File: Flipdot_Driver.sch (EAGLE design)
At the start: 27 parts

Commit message: Finished driver board design
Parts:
- added U$6: 3_PIN, Flipdot:3_PIN
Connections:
- net A: now also U$6.1
- net B: now also U$6.2
- net C: now also U$6.3
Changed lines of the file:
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@@
 <part name="U$11" library="Flipdot" deviceset="4_PIN" device=""/>
 <part name="U$5" library="Flipdot" deviceset="3_PIN" device=""/>
+<part name="U$6" library="Flipdot" deviceset="3_PIN" device=""/>
 </parts>
 <sheets>
@@
 <instance part="U$11" gate="G$1" x="-114.3" y="-144.78" rot="MR0"/>
 <instance part="U$5" gate="G$1" x="-22.86" y="-40.64" rot="MR0"/>
+<instance part="U$6" gate="G$1" x="-78.74" y="-2.54" rot="R180"/>
 </instances>
 <busses>
@@
 <label x="-40.64" y="7.62" size="1.778" layer="95"/>
 </segment>
+<segment>
+<pinref part="U$6" gate="G$1" pin="1"/>
+<wire x1="-60.96" y1="-7.62" x2="-73.66" y2="-7.62" width="0.1524" layer="91"/>
+<label x="-73.66" y="-7.62" size="1.778" layer="95"/>
+</segment>
 </net>
 <net name="B" class="0">
@@
 <wire x1="-38.1" y1="2.54" x2="-40.64" y2="2.54" width="0.1524" layer="91"/>
 <label x="-40.64" y="2.54" size="1.778" layer="95"/>
+</segment>
+<segment>
+<pinref part="U$6" gate="G$1" pin="2"/>
+<wire x1="-60.96" y1="-2.54" x2="-73.66" y2="-2.54" width="0.1524" layer="91"/>
+<label x="-73.66" y="-2.54" size="1.778" layer="95"/>
 </segment>
 </net>
@@
 <label x="-40.64" y="-2.54" size="1.778" layer="95"/>
 </segment>
-</net>
+<segment>
+<pinref part="U$6" gate="G$1" pin="3"/>
+<wire x1="-60.96" y1="2.54" x2="-73.66" y2="2.54" width="0.1524" layer="91"/>
+<label x="-73.66" y="2.54" size="1.778" layer="95"/>
+</segment>
+</net>

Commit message: Finished, sent for production review
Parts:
- removed U$6: 3_PIN, Flipdot:3_PIN
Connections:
- net A: no longer U$6.1
- net B: no longer U$6.2
- net C: no longer U$6.3
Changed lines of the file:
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@@
 <?xml version="1.0" encoding="utf-8"?>
 <!DOCTYPE eagle SYSTEM "eagle.dtd">
-<eagle version="9.1.3">
+<eagle version="9.2.2">
 <drawing>
 <settings>
@@
 <part name="U$11" library="Flipdot" deviceset="4_PIN" device=""/>
 <part name="U$5" library="Flipdot" deviceset="3_PIN" device=""/>
-<part name="U$6" library="Flipdot" deviceset="3_PIN" device=""/>
 </parts>
 <sheets>
@@
 </plain>
 <instances>
-<instance part="SUBSEG" gate="G$1" x="-15.24" y="-137.16" rot="R270"/>
-<instance part="COL_A_H" gate="G$1" x="66.04" y="-137.16" rot="R270"/>
-<instance part="COL_A_L" gate="G$1" x="66.04" y="-187.96" rot="R270"/>
-<instance part="COL_B_H" gate="G$1" x="66.04" y="-243.84" rot="R270"/>
-<instance part="COL_B_L" gate="G$1" x="66.04" y="-294.64" rot="R270"/>
-<instance part="COL_C_H" gate="G$1" x="66.04" y="-350.52" rot="R270"/>
-<instance part="COL_C_L" gate="G$1" x="66.04" y="-401.32" rot="R270"/>
-<instance part="COL_D_HL" gate="G$1" x="66.04" y="-457.2" rot="R270"/>
-<instance part="SOURCE_A" gate="G$1" x="124.46" y="-142.24" rot="R270"/>
-<instance part="SOURCE_B" gate="G$1" x="124.46" y="-248.92" rot="R270"/>
-<instance part="SOURCE_C" gate="G$1" x="124.46" y="-355.6" rot="R270"/>
-<instance part="SOURCE_D" gate="G$1" x="124.46" y="-462.28" rot="R270"/>
-<instance part="SINK_B" gate="G$1" x="124.46" y="-299.72" rot="R270"/>
-<instance part="SINK_C" gate="G$1" x="124.46" y="-406.4" rot="R270"/>
-<instance part="SINK_D" gate="G$1" x="124.46" y="-523.24" rot="R270"/>
-<instance part="SINK_A" gate="G$1" x="124.46" y="-193.04" rot="R270"/>
-<instance part="U$1" gate="G$1" x="302.26" y="-231.14" rot="R90"/>
-<instance part="ROW_L" gate="G$1" x="119.38" y="20.32" rot="R270"/>
-<instance part="ROW_H" gate="G$1" x="119.38" y="-33.02" rot="R270"/>
-<instance part="SINK_R" gate="G$1" x="172.72" y="10.16" rot="R270"/>
-<instance part="SOURCE_R" gate="G$1" x="172.72" y="-43.18" rot="R270"/>
-<instance part="U$2" gate="G$1" x="-33.02" y="2.54"/>
-<instance part="U$3" gate="G$1" x="-43.18" y="-124.46" rot="MR0"/>
-<instance part="U$4" gate="G$1" x="68.58" y="33.02" rot="R180"/>
-<instance part="U$10" gate="G$1" x="-81.28" y="-144.78"/>
-<instance part="U$11" gate="G$1" x="-114.3" y="-144.78" rot="MR0"/>
-<instance part="U$5" gate="G$1" x="-22.86" y="-40.64" rot="MR0"/>
-<instance part="U$6" gate="G$1" x="-78.74" y="-2.54" rot="R180"/>
+<instance part="SUBSEG" gate="G$1" x="-15.24" y="-137.16" smashed="yes" rot="R270">
+<attribute name="NAME" x="-20.32" y="-160.02" size="1.778" layer="94"/>
+</instance>
+<instance part="COL_A_H" gate="G$1" x="66.04" y="-137.16" smashed="yes" rot="R270">
+<attribute name="NAME" x="60.96" y="-160.02" size="1.778" layer="94"/>
+</instance>
+<instance part="COL_A_L" gate="G$1" x="66.04" y="-187.96" smashed="yes" rot="R270">
+<attribute name="NAME" x="60.96" y="-210.82" size="1.778" layer="94"/>
+</instance>
+<instance part="COL_B_H" gate="G$1" x="66.04" y="-243.84" smashed="yes" rot="R270">
+<attribute name="NAME" x="60.96" y="-266.7" size="1.778" layer="94"/>
+</instance>
+<instance part="COL_B_L" gate="G$1" x="66.04" y="-294.64" smashed="yes" rot="R270">
+<attribute name="NAME" x="60.96" y="-317.5" size="1.778" layer="94"/>
+</instance>
+<instance part="COL_C_H" gate="G$1" x="66.04" y="-350.52" smashed="yes" rot="R270">
+<attribute name="NAME" x="60.96" y="-373.38" size="1.778" layer="94"/>
+</instance>
+<instance part="COL_C_L" gate="G$1" x="66.04" y="-401.32" smashed="yes" rot="R270">
+<attribute name="NAME" x="60.96" y="-424.18" size="1.778" layer="94"/>
+</instance>
+<instance part="COL_D_HL" gate="G$1" x="66.04" y="-457.2" smashed="yes" rot="R270">
+<attribute name="NAME" x="60.96" y="-480.06" size="1.778" layer="94"/>
+</instance>
+<instance part="SOURCE_A" gate="G$1" x="124.46" y="-142.24" smashed="yes" rot="R270">
+<attribute name="NAME" x="119.38" y="-170.18" size="1.778" layer="94"/>
+</instance>
+<instance part="SOURCE_B" gate="G$1" x="124.46" y="-248.92" smashed="yes" rot="R270">
+<attribute name="NAME" x="119.38" y="-276.86" size="1.778" layer="94"/>
+</instance>
+<instance part="SOURCE_C" gate="G$1" x="124.46" y="-355.6" smashed="yes" rot="R270">
+<attribute name="NAME" x="119.38" y="-383.54" size="1.778" layer="94"/>
+</instance>
+<instance part="SOURCE_D" gate="G$1" x="124.46" y="-462.28" smashed="yes" rot="R270">
+<attribute name="NAME" x="119.38" y="-490.22" size="1.778" layer="94"/>
+</instance>
+<instance part="SINK_B" gate="G$1" x="124.46" y="-299.72" smashed="yes" rot="R270">
+<attribute name="NAME" x="119.38" y="-322.58" size="1.778" layer="94"/>
+</instance>
+<instance part="SINK_C" gate="G$1" x="124.46" y="-406.4" smashed="yes" rot="R270">
+<attribute name="NAME" x="119.38" y="-429.26" size="1.778" layer="94"/>
+</instance>
+<instance part="SINK_D" gate="G$1" x="124.46" y="-523.24" smashed="yes" rot="R270">
+<attribute name="NAME" x="119.38" y="-546.1" size="1.778" layer="94"/>
+</instance>
+<instance part="SINK_A" gate="G$1" x="124.46" y="-193.04" smashed="yes" rot="R270">
+<attribute name="NAME" x="119.38" y="-215.9" size="1.778" layer="94"/>
+</instance>
+<instance part="U$1" gate="G$1" x="302.26" y="-231.14" smashed="yes" rot="R90"/>
+<instance part="ROW_L" gate="G$1" x="119.38" y="20.32" smashed="yes" rot="R270">
+<attribute name="NAME" x="114.3" y="-2.54" size="1.778" layer="94"/>
+</instance>
+<instance part="ROW_H" gate="G$1" x="119.38" y="-33.02" smashed="yes" rot="R270">
+<attribute name="NAME" x="114.3" y="-55.88" size="1.778" layer="94"/>
+</instance>
+<instance part="SINK_R" gate="G$1" x="172.72" y="10.16" smashed="yes" rot="R270">
+<attribute name="NAME" x="167.64" y="-12.7" size="1.778" layer="94"/>
+</instance>
+<instance part="SOURCE_R" gate="G$1" x="172.72" y="-43.18" smashed="yes" rot="R270">
+<attribute name="NAME" x="167.64" y="-71.12" size="1.778" layer="94"/>
+</instance>
+<instance part="U$2" gate="G$1" x="-33.02" y="2.54" smashed="yes"/>
+<instance part="U$3" gate="G$1" x="-43.18" y="-124.46" smashed="yes" rot="MR0"/>
+<instance part="U$4" gate="G$1" x="68.58" y="33.02" smashed="yes" rot="R180"/>
+<instance part="U$10" gate="G$1" x="-81.28" y="-144.78" smashed="yes"/>
+<instance part="U$11" gate="G$1" x="-114.3" y="-144.78" smashed="yes" rot="MR0"/>
+<instance part="U$5" gate="G$1" x="-22.86" y="-40.64" smashed="yes" rot="MR0"/>
 </instances>
 <busses>
@@
 <label x="-40.64" y="7.62" size="1.778" layer="95"/>
 </segment>
-<segment>
-<pinref part="U$6" gate="G$1" pin="1"/>
-<wire x1="-60.96" y1="-7.62" x2="-73.66" y2="-7.62" width="0.1524" layer="91"/>
-<label x="-73.66" y="-7.62" size="1.778" layer="95"/>
-</segment>
 </net>
 <net name="B" class="0">
@@
 <wire x1="-38.1" y1="2.54" x2="-40.64" y2="2.54" width="0.1524" layer="91"/>
 <label x="-40.64" y="2.54" size="1.778" layer="95"/>
-</segment>
-<segment>
-<pinref part="U$6" gate="G$1" pin="2"/>
-<wire x1="-60.96" y1="-2.54" x2="-73.66" y2="-2.54" width="0.1524" layer="91"/>
-<label x="-73.66" y="-2.54" size="1.778" layer="95"/>
 </segment>
 </net>
@@
 <label x="-40.64" y="-2.54" size="1.778" layer="95"/>
 </segment>
-<segment>
-<pinref part="U$6" gate="G$1" pin="3"/>
-<wire x1="-60.96" y1="2.54" x2="-73.66" y2="2.54" width="0.1524" layer="91"/>
-<label x="-73.66" y="2.54" size="1.778" layer="95"/>
-</segment>
-</net>
+</net>

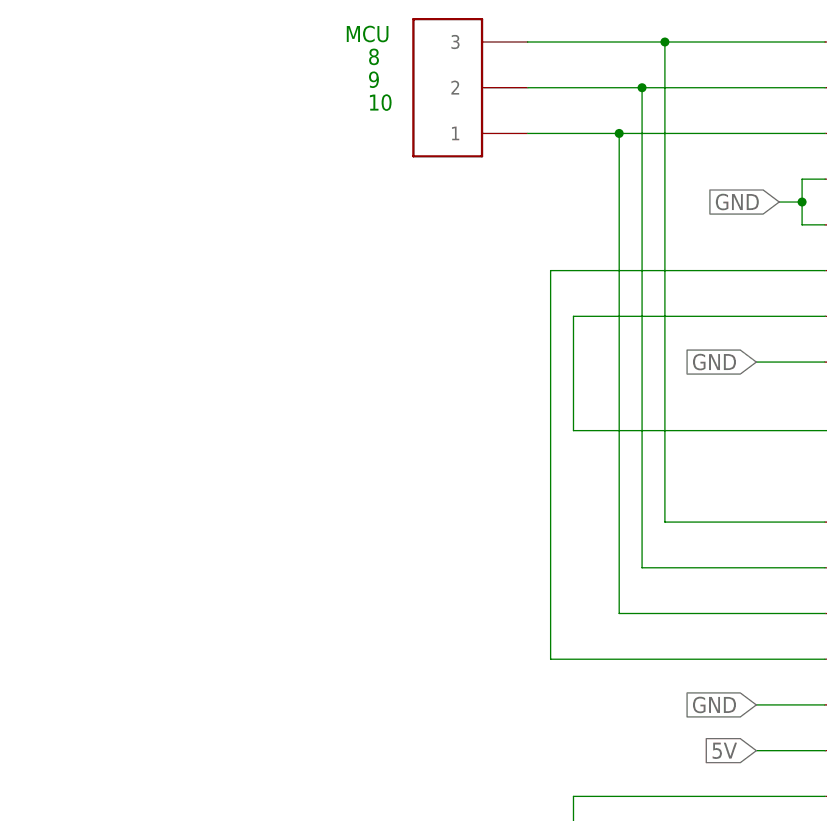
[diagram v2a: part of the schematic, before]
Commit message: Fixed missing RE connector
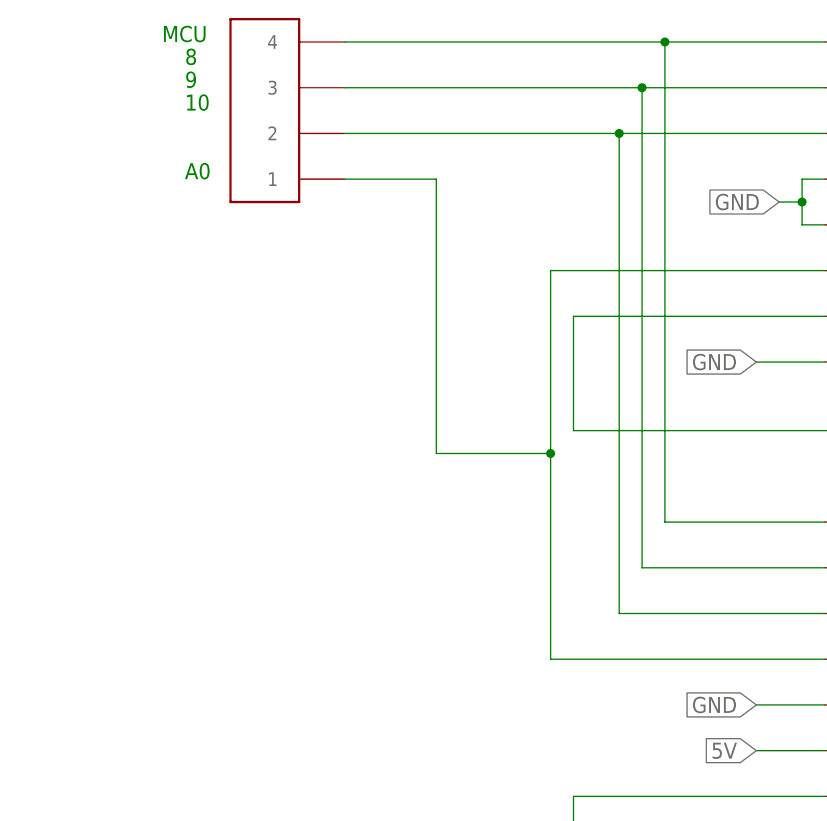
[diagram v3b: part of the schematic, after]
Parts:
- removed U$4: 3_PIN, Flipdot:3_PIN
- added U$6: 4_PIN, Flipdot:4_PIN
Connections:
- net N$62: now also U$6.4; no longer U$4.3
- net N$63: now also U$6.3; no longer U$4.2
- net N$64: now also U$6.2; no longer U$4.1
- net N$65: now also U$6.1
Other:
- note added: "A0"
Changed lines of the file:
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@@
 <part name="U$2" library="Flipdot" deviceset="3_PIN" device=""/>
 <part name="U$3" library="Flipdot" deviceset="3_PIN" device=""/>
-<part name="U$4" library="Flipdot" deviceset="3_PIN" device=""/>
 <part name="U$10" library="Flipdot" deviceset="JUMPER" device=""/>
 <part name="U$11" library="Flipdot" deviceset="4_PIN" device=""/>
 <part name="U$5" library="Flipdot" deviceset="3_PIN" device=""/>
+<part name="U$6" library="Flipdot" deviceset="4_PIN" device=""/>
 </parts>
 <sheets>
@@
 <text x="-55.88" y="-127" size="1.778" layer="91">7</text>
 <text x="-58.42" y="-119.38" size="1.778" layer="91">MCU</text>
-<text x="55.88" y="35.56" size="1.778" layer="91">8</text>
-<text x="55.88" y="33.02" size="1.778" layer="91">9</text>
-<text x="55.88" y="30.48" size="1.778" layer="91">10</text>
-<text x="53.34" y="38.1" size="1.778" layer="91">MCU</text>
+<text x="35.56" y="35.56" size="1.778" layer="91">8</text>
+<text x="35.56" y="33.02" size="1.778" layer="91">9</text>
+<text x="35.56" y="30.48" size="1.778" layer="91">10</text>
+<text x="33.02" y="38.1" size="1.778" layer="91">MCU</text>
+<text x="35.56" y="22.86" size="1.778" layer="91">A0</text>
 </plain>
 <instances>
@@
 <instance part="U$2" gate="G$1" x="-33.02" y="2.54" smashed="yes"/>
 <instance part="U$3" gate="G$1" x="-43.18" y="-124.46" smashed="yes" rot="MR0"/>
-<instance part="U$4" gate="G$1" x="68.58" y="33.02" smashed="yes" rot="R180"/>
 <instance part="U$10" gate="G$1" x="-81.28" y="-144.78" smashed="yes"/>
 <instance part="U$11" gate="G$1" x="-114.3" y="-144.78" smashed="yes" rot="MR0"/>
 <instance part="U$5" gate="G$1" x="-22.86" y="-40.64" smashed="yes" rot="MR0"/>
+<instance part="U$6" gate="G$1" x="48.26" y="30.48" smashed="yes" rot="R180"/>
 </instances>
 <busses>
@@
 <pinref part="ROW_H" gate="G$1" pin="A0"/>
 <wire x1="88.9" y1="-15.24" x2="106.68" y2="-15.24" width="0.1524" layer="91"/>
-<pinref part="U$4" gate="G$1" pin="3"/>
-<wire x1="73.66" y1="38.1" x2="88.9" y2="38.1" width="0.1524" layer="91"/>
+<wire x1="53.34" y1="38.1" x2="88.9" y2="38.1" width="0.1524" layer="91"/>
 <junction x="88.9" y="38.1"/>
+<pinref part="U$6" gate="G$1" pin="4"/>
 </segment>
 </net>
@@
 <wire x1="86.36" y1="33.02" x2="86.36" y2="-20.32" width="0.1524" layer="91"/>
 <wire x1="86.36" y1="-20.32" x2="106.68" y2="-20.32" width="0.1524" layer="91"/>
-<pinref part="U$4" gate="G$1" pin="2"/>
-<wire x1="73.66" y1="33.02" x2="86.36" y2="33.02" width="0.1524" layer="91"/>
+<wire x1="53.34" y1="33.02" x2="86.36" y2="33.02" width="0.1524" layer="91"/>
 <junction x="86.36" y="33.02"/>
+<pinref part="U$6" gate="G$1" pin="3"/>
 </segment>
 </net>
@@
 <wire x1="83.82" y1="27.94" x2="83.82" y2="-25.4" width="0.1524" layer="91"/>
 <wire x1="83.82" y1="-25.4" x2="106.68" y2="-25.4" width="0.1524" layer="91"/>
-<pinref part="U$4" gate="G$1" pin="1"/>
-<wire x1="73.66" y1="27.94" x2="83.82" y2="27.94" width="0.1524" layer="91"/>
+<wire x1="53.34" y1="27.94" x2="83.82" y2="27.94" width="0.1524" layer="91"/>
 <junction x="83.82" y="27.94"/>
+<pinref part="U$6" gate="G$1" pin="2"/>
 </segment>
 </net>
@@
 <pinref part="ROW_H" gate="G$1" pin="!E1"/>
 <wire x1="106.68" y1="-30.48" x2="76.2" y2="-30.48" width="0.1524" layer="91"/>
-<wire x1="76.2" y1="-30.48" x2="76.2" y2="12.7" width="0.1524" layer="91"/>
-</segment>
-</net>
+<wire x1="76.2" y1="-30.48" x2="76.2" y2="-7.62" width="0.1524" layer="91"/>
+<wire x1="76.2" y1="-7.62" x2="76.2" y2="12.7" width="0.1524" layer="91"/>
+<wire x1="76.2" y1="-7.62" x2="63.5" y2="-7.62" width="0.1524" layer="91"/>
+<junction x="76.2" y="-7.62"/>
+<pinref part="U$6" gate="G$1" pin="1"/>
+<wire x1="63.5" y1="-7.62" x2="63.5" y2="22.86" width="0.1524" layer="91"/>
+<wire x1="63.5" y1="22.86" x2="53.34" y2="22.86" width="0.1524" layer="91"/>
+</segment>
+</net>
